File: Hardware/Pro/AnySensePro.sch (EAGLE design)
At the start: 63 parts, among them U1 LP2992IM5-3.3, U2 BLUENRGQTR, U3 SN65HVD232D, U4 STM32F303RET6, U5 BALF-NRG-01D3, U6 M25P16VMN6P, X6 MEM2051-00-195-00-A, X7 TC2030-IDC-NL, Y1 ABM3B, Y2 ABM8, Y3 ABS07

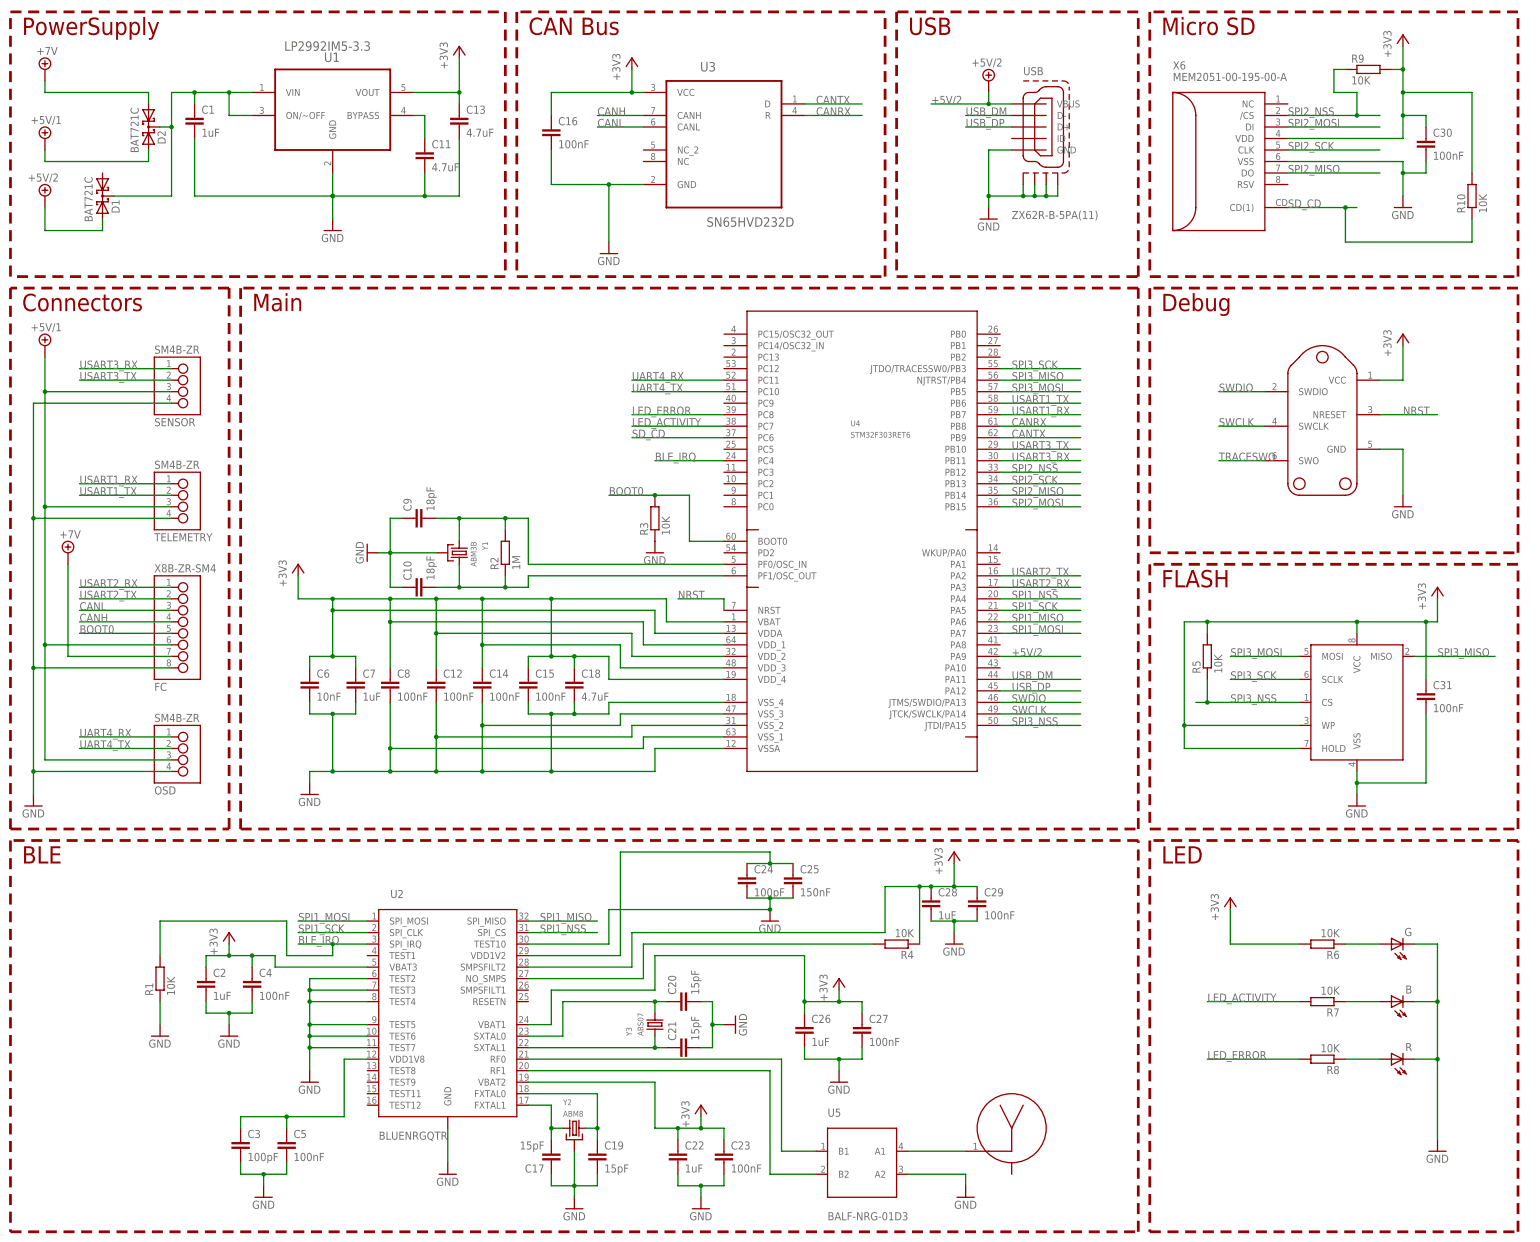
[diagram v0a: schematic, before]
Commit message: Order Codes added
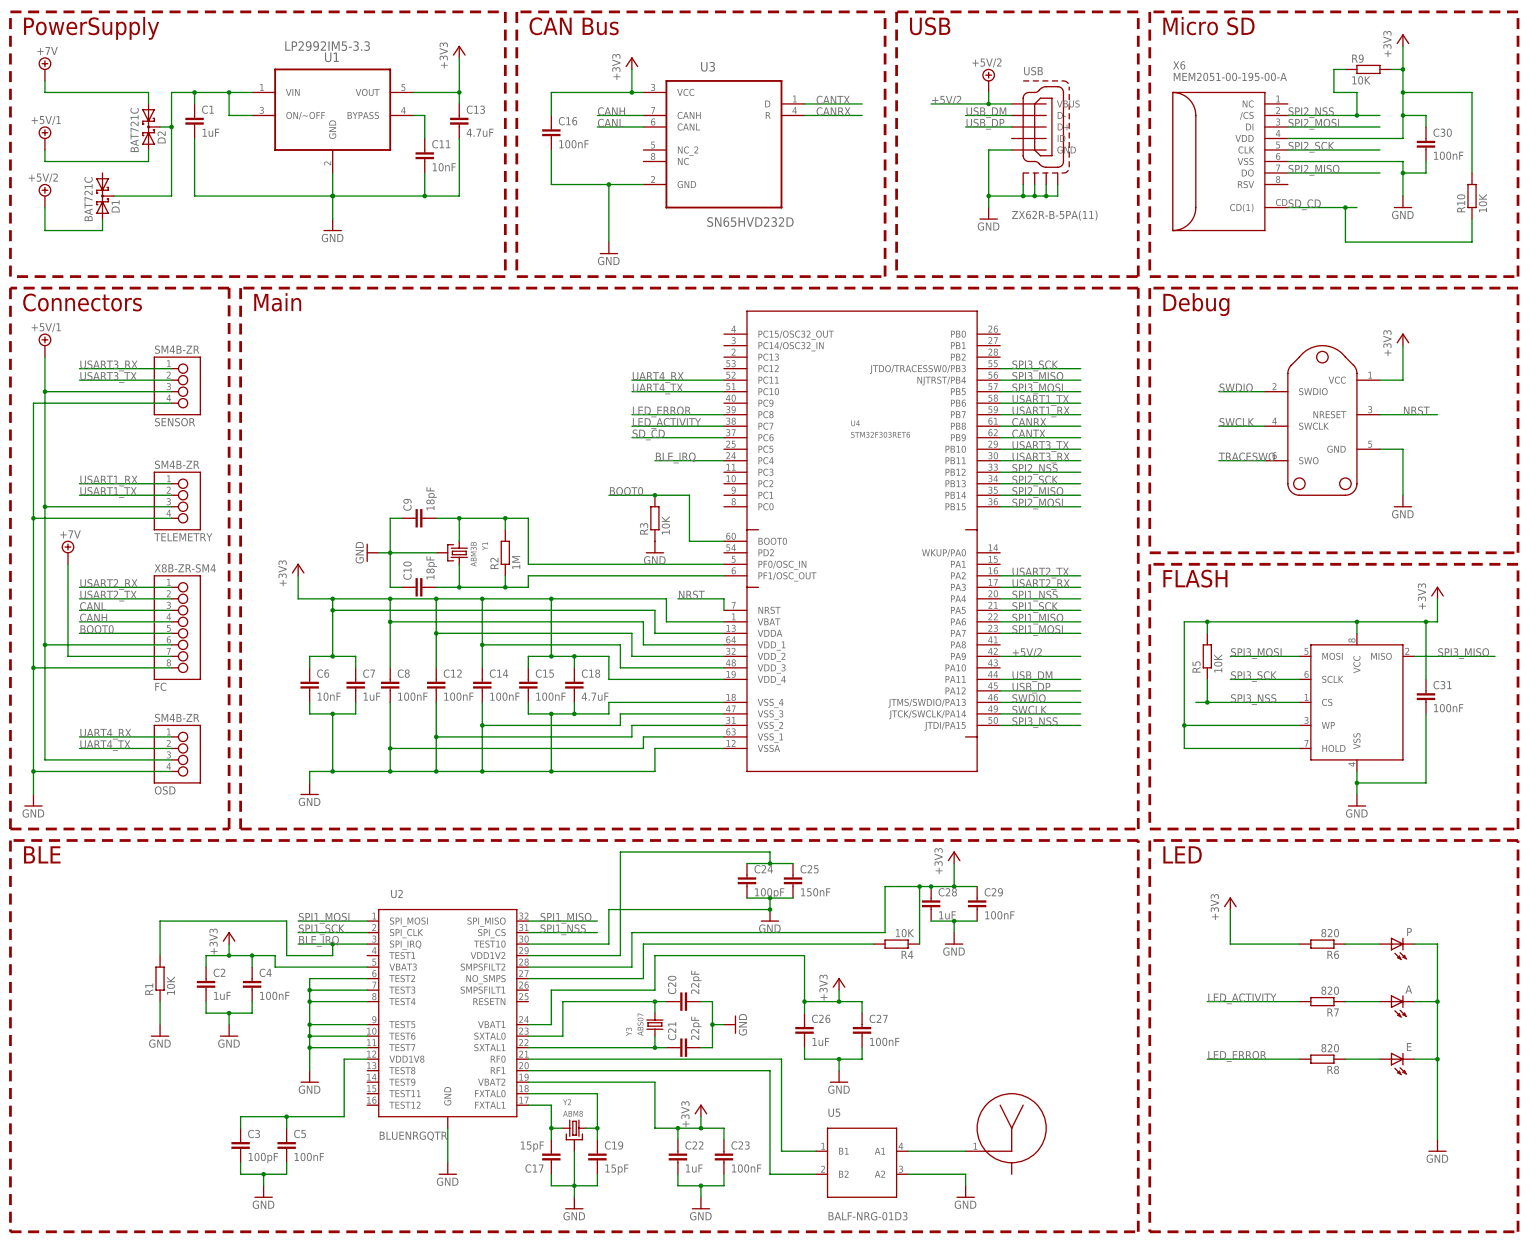
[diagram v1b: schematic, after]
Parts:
- A: OC_FARNELL 2217978 -> 2468793RL
- C1, C2, C22, C26, C28, C7: OC_FARNELL (none) -> 2362093RL
- C10, C9: OC_FARNELL (none) -> 1758947RL
- C11: value 4.7uF -> 10nF; OC_FARNELL (none) -> 1758924RL
- C12, C14, C15, C16, C23, C27, C29, C30, C31, C4, C5: OC_FARNELL (none) -> 1759380RL
- C13, C18: OC_FARNELL (none) -> 2426952RL
- C17, C19: OC_FARNELL (none) -> 1758945RL
- C20, C21: value 15pF -> 22pF; OC_FARNELL (none) -> 1758951RL
- C24, C3: OC_FARNELL (none) -> 2320762RL
- C25: OC_FARNELL (none) -> 2470467RL
- C6: OC_FARNELL (none) -> 1758924RL
- C8: OC_FARNELL test -> 1759380RL
- E: OC_FARNELL 2099224 -> 2468792RL
- P: OC_FARNELL 2099223RL -> 2468791RL
- R1, R10, R3, R4, R5, R9: OC_FARNELL (none) -> 2302739RL
- R2: OC_FARNELL (none) -> 2302957RL
- R6, R7, R8: value 10K -> 820; OC_FARNELL (none) -> 2302628RL
- renumbered B to A, G to P, R to E

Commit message: Hardware redesign
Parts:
- removed A1: 2450AT18A100, johanson-technology:2450AT18A100
- removed C17, C19: 15pF, rcl:C-EUC0402K
- removed C2, C22, C26, C28: 1uF, rcl:C-EUC0402K
- removed C20, C21: 22pF, rcl:C-EUC0402K
- removed C23, C27, C29, C4, C5: 100nF, rcl:C-EUC0402K
- removed C24, C3: 100pF, rcl:C-EUC0402K
- removed C25: 150nF, rcl:C-EUC0402K
- removed U2: BLUENRGQTR, ST-Microelctronics:BLUENRGQTR
- removed U5: BALF-NRG-01D3, ST-Microelctronics:BALF-NRG-01D3
- removed Y2: ABM8, abracon:ABM8-16.000MHZ-10-1-U-T
- removed Y3: ABS07, abracon:ABS.ABS07
- added R11: 22R, rcl:R-EU_R0402
- added R12: 10K, rcl:R-EU_R0402
- added R13: 15K, rcl:R-EU_R0402
- C1: device rcl:C-EUC0402K -> rcl:C-EUC0603K; OC_FARNELL 2362093RL -> 1759409RL
- C13, C18: device rcl:C-EUC0402K -> rcl:C-EUC0603K; OC_FARNELL 2426952RL -> 2320818RL
- C7: OC_FARNELL 2362093RL -> 2320776RL
- R1: value 10K -> 22R
- R4: value 10K -> 1.5K
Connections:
- removed net BLE_IRQ: R1.2, U2.SPI_IRQ, U4.PC4
- removed net N$10: C19.1, U2.FXTAL0, Y2.2
- removed net N$11: C17.2, U2.FXTAL1, Y2.1
- removed net N$12: C3.1, C5.1, U2.VDD1V8
- removed net N$13: C20.1, U2.SXTAL0, Y3.2
- removed net N$14: C21.1, U2.SXTAL1, Y3.1
- removed net N$2: U2.RF0, U5.B1
- removed net N$3: U2.RF1, U5.B2
- removed net N$4: C24.1, C25.1, U2.VDD1V2
- removed net N$5: R4.2, U2.NO_SMPS
- removed net N$9: A1.1, U5.A1
- removed net SPI2_MISO: U4.PB14, X6.DO
- removed net SPI2_MOSI: U4.PB15, X6.DI
- removed net SPI2_NSS: R9.1, U4.PB12, X6./CS
- removed net SPI2_SCK: U4.PB13, X6.CLK
- new net USB_D+: R1.2, R4.1, USBG$1.D+
- new net USB_D-: R11.2, USBG$1.D-
- new net USB_DISCONNECT: R4.2, U4.PA8
- new net USB_SENSE: R12.1, R13.2, U4.PB15
- net +3V3: no longer C2.1, C22.1, C23.1, C26.1, C27.1, C28.1, C29.1, C4.1, R4.1, U2.SMPSFILT2, U2.VBAT1, U2.VBAT2, U2.VBAT3
- net +5V/2: now also R12.2; no longer U4.PA9
- net GND: now also R13.1; no longer C17.1, C19.2, C2.2, C20.2, C21.2, C22.2, C23.2, C24.2, C25.2, C26.2, C27.2, C28.2, C29.2, C3.2, C4.2, C5.2, R1.1, U2.GND, U2.TEST10, U2.TEST2, U2.TEST3, U2.TEST4, U2.TEST5, U2.TEST6, U2.TEST7, U5.A2, Y2.GND
- net LED_ACTIVITY: now also U4.PC3; no longer U4.PC7
- net LED_ERROR: now also U4.PC2; no longer U4.PC8
- net SD_CD: now also U4.PC4; no longer U4.PC6
- net SPI1_MISO: now also X6.DO; no longer U2.SPI_MISO
- net SPI1_MOSI: now also X6.DI; no longer U2.SPI_MOSI
- net SPI1_NSS: now also R9.1, X6./CS; no longer U2.SPI_CS
- net SPI1_SCK: now also X6.CLK; no longer U2.SPI_CLK
- net USART1_RX: now also U4.PA10; no longer U4.PB7
- net USART1_TX: now also U4.PA9; no longer U4.PB6
- net USB_DM: now also R11.1; no longer USBG$1.D-
- net USB_DP: now also R1.1; no longer USBG$1.D+
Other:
- note removed: "BLE"
- moved on the sheet: A, C30, C31, E, P, R1, R10, R4, R5, R6, R7, R8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

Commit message: AnySense Pro V1.1
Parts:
- renumbered TELEMETRY to TELEM
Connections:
- net USB_SENSE: now also U4.PC0; no longer U4.PB15
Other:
- moved on the sheet: R3
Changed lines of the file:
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@@
 <grid distance="0.1" unitdist="inch" unit="inch" style="lines" multiple="1" display="no" altdistance="0.01" altunitdist="inch" altunit="inch"/>
 <layers>
-<layer number="1" name="Top" color="4" fill="1" visible="yes" active="no"/>
-<layer number="16" name="Bottom" color="1" fill="1" visible="yes" active="no"/>
-<layer number="17" name="Pads" color="2" fill="1" visible="yes" active="no"/>
-<layer number="18" name="Vias" color="2" fill="1" visible="yes" active="no"/>
-<layer number="19" name="Unrouted" color="6" fill="1" visible="yes" active="no"/>
-<layer number="20" name="Dimension" color="15" fill="1" visible="yes" active="no"/>
-<layer number="21" name="tPlace" color="7" fill="1" visible="yes" active="no"/>
-<layer number="22" name="bPlace" color="7" fill="1" visible="yes" active="no"/>
-<layer number="23" name="tOrigins" color="15" fill="1" visible="yes" active="no"/>
-<layer number="24" name="bOrigins" color="15" fill="1" visible="yes" active="no"/>
-<layer number="25" name="tNames" color="7" fill="1" visible="yes" active="no"/>
-<layer number="26" name="bNames" color="7" fill="1" visible="yes" active="no"/>
-<layer number="27" name="tValues" color="7" fill="1" visible="yes" active="no"/>
-<layer number="28" name="bValues" color="7" fill="1" visible="yes" active="no"/>
+<layer number="1" name="Top" color="4" fill="1" visible="no" active="no"/>
+<layer number="16" name="Bottom" color="1" fill="1" visible="no" active="no"/>
+<layer number="17" name="Pads" color="2" fill="1" visible="no" active="no"/>
+<layer number="18" name="Vias" color="2" fill="1" visible="no" active="no"/>
+<layer number="19" name="Unrouted" color="6" fill="1" visible="no" active="no"/>
+<layer number="20" name="Dimension" color="15" fill="1" visible="no" active="no"/>
+<layer number="21" name="tPlace" color="7" fill="1" visible="no" active="no"/>
+<layer number="22" name="bPlace" color="7" fill="1" visible="no" active="no"/>
+<layer number="23" name="tOrigins" color="15" fill="1" visible="no" active="no"/>
+<layer number="24" name="bOrigins" color="15" fill="1" visible="no" active="no"/>
+<layer number="25" name="tNames" color="7" fill="1" visible="no" active="no"/>
+<layer number="26" name="bNames" color="7" fill="1" visible="no" active="no"/>
+<layer number="27" name="tValues" color="7" fill="1" visible="no" active="no"/>
+<layer number="28" name="bValues" color="7" fill="1" visible="no" active="no"/>
 <layer number="29" name="tStop" color="7" fill="3" visible="no" active="no"/>
 <layer number="30" name="bStop" color="7" fill="6" visible="no" active="no"/>
@@
 <layer number="35" name="tGlue" color="7" fill="4" visible="no" active="no"/>
 <layer number="36" name="bGlue" color="7" fill="5" visible="no" active="no"/>
-<layer number="37" name="tTest" color="7" fill="1" visible="yes" active="no"/>
-<layer number="38" name="bTest" color="7" fill="1" visible="yes" active="no"/>
+<layer number="37" name="tTest" color="7" fill="1" visible="no" active="no"/>
+<layer number="38" name="bTest" color="7" fill="1" visible="no" active="no"/>
 <layer number="39" name="tKeepout" color="4" fill="11" visible="no" active="no"/>
 <layer number="40" name="bKeepout" color="1" fill="11" visible="no" active="no"/>
@@
 <layer number="44" name="Drills" color="7" fill="1" visible="no" active="no"/>
 <layer number="45" name="Holes" color="7" fill="1" visible="no" active="no"/>
-<layer number="46" name="Milling" color="3" fill="1" visible="yes" active="no"/>
-<layer number="47" name="Measures" color="7" fill="1" visible="yes" active="no"/>
-<layer number="48" name="Document" color="7" fill="1" visible="yes" active="no"/>
-<layer number="49" name="Reference" color="7" fill="1" visible="yes" active="no"/>
-<layer number="50" name="dxf" color="7" fill="1" visible="yes" active="no"/>
-<layer number="51" name="tDocu" color="7" fill="1" visible="yes" active="no"/>
-<layer number="52" name="bDocu" color="7" fill="1" visible="yes" active="no"/>
-<layer number="53" name="tGND_GNDA" color="7" fill="9" visible="yes" active="no"/>
-<layer number="54" name="bGND_GNDA" color="1" fill="9" visible="yes" active="no"/>
-<layer number="56" name="wert" color="7" fill="1" visible="yes" active="no"/>
+<layer number="46" name="Milling" color="3" fill="1" visible="no" active="no"/>
+<layer number="47" name="Measures" color="7" fill="1" visible="no" active="no"/>
+<layer number="48" name="Document" color="7" fill="1" visible="no" active="no"/>
+<layer number="49" name="Reference" color="7" fill="1" visible="no" active="no"/>
+<layer number="50" name="dxf" color="7" fill="1" visible="no" active="no"/>
+<layer number="51" name="tDocu" color="7" fill="1" visible="no" active="no"/>
+<layer number="52" name="bDocu" color="7" fill="1" visible="no" active="no"/>
+<layer number="53" name="tGND_GNDA" color="7" fill="9" visible="no" active="no"/>
+<layer number="54" name="bGND_GNDA" color="1" fill="9" visible="no" active="no"/>
+<layer number="56" name="wert" color="7" fill="1" visible="no" active="no"/>
 <layer number="90" name="Modules" color="5" fill="1" visible="yes" active="yes"/>
 <layer number="91" name="Nets" color="2" fill="1" visible="yes" active="yes"/>
@@
 <parts>
 <part name="X6" library="con-gct" deviceset="MEM2051" device="-00-195-00-A"/>
-<part name="TELEMETRY" library="con-jst" deviceset="?4B-ZR" device="SM"/>
+<part name="TELEM" library="con-jst" deviceset="?4B-ZR" device="SM"/>
 <part name="SENSOR" library="con-jst" deviceset="?4B-ZR" device="SM"/>
 <part name="OSD" library="con-jst" deviceset="?4B-ZR" device="SM"/>
@@
 <instances>
 <instance part="X6" gate="G$1" x="269.24" y="147.32"/>
-<instance part="TELEMETRY" gate="1" x="38.1" y="132.08"/>
+<instance part="TELEM" gate="1" x="38.1" y="132.08"/>
 <instance part="SENSOR" gate="1" x="38.1" y="157.48"/>
 <instance part="OSD" gate="1" x="38.1" y="76.2"/>
@@
 <instance part="FC" gate="G$1" x="38.1" y="106.68"/>
 <instance part="SUPPLY5" gate="G$1" x="12.7" y="121.92"/>
-<instance part="R3" gate="G$1" x="142.24" y="129.54" rot="R90">
-<attribute name="OC_FARNELL" x="142.24" y="129.54" size="1.778" layer="96" rot="R90" display="off"/>
-</instance>
-<instance part="GND12" gate="1" x="142.24" y="121.92"/>
+<instance part="R3" gate="G$1" x="121.92" y="129.54" rot="R90">
+<attribute name="OC_FARNELL" x="121.92" y="129.54" size="1.778" layer="96" rot="R90" display="off"/>
+</instance>
+<instance part="GND12" gate="1" x="121.92" y="121.92"/>
 <instance part="C16" gate="G$1" x="119.38" y="215.9">
 <attribute name="OC_FARNELL" x="119.38" y="215.9" size="1.778" layer="96" display="off"/>
@@
 <segment>
 <pinref part="GND1" gate="1" pin="GND"/>
-<pinref part="TELEMETRY" gate="1" pin="4"/>
+<pinref part="TELEM" gate="1" pin="4"/>
 <wire x1="5.08" y1="68.58" x2="5.08" y2="73.66" width="0.1524" layer="91"/>
 <wire x1="5.08" y1="73.66" x2="5.08" y2="96.52" width="0.1524" layer="91"/>
@@
 <net name="+5V/1" class="0">
 <segment>
-<pinref part="TELEMETRY" gate="1" pin="3"/>
+<pinref part="TELEM" gate="1" pin="3"/>
 <wire x1="35.56" y1="132.08" x2="7.62" y2="132.08" width="0.1524" layer="91"/>
 <wire x1="7.62" y1="132.08" x2="7.62" y2="157.48" width="0.1524" layer="91"/>
@@
 <net name="USART1_RX" class="0">
 <segment>
-<pinref part="TELEMETRY" gate="1" pin="1"/>
+<pinref part="TELEM" gate="1" pin="1"/>
 <wire x1="35.56" y1="137.16" x2="15.24" y2="137.16" width="0.1524" layer="91"/>
 <label x="15.24" y="137.16" size="1.778" layer="95"/>
@@
 <net name="USART1_TX" class="0">
 <segment>
-<pinref part="TELEMETRY" gate="1" pin="2"/>
+<pinref part="TELEM" gate="1" pin="2"/>
 <wire x1="35.56" y1="134.62" x2="15.24" y2="134.62" width="0.1524" layer="91"/>
 <label x="15.24" y="134.62" size="1.778" layer="95"/>
@@
 <segment>
 <pinref part="U4" gate="G$1" pin="BOOT0"/>
-<wire x1="157.48" y1="124.46" x2="149.86" y2="124.46" width="0.1524" layer="91"/>
-<wire x1="149.86" y1="124.46" x2="149.86" y2="134.62" width="0.1524" layer="91"/>
+<wire x1="157.48" y1="124.46" x2="129.54" y2="124.46" width="0.1524" layer="91"/>
+<wire x1="129.54" y1="124.46" x2="129.54" y2="134.62" width="0.1524" layer="91"/>
 <pinref part="R3" gate="G$1" pin="2"/>
-<wire x1="149.86" y1="134.62" x2="142.24" y2="134.62" width="0.1524" layer="91"/>
-<wire x1="142.24" y1="134.62" x2="132.08" y2="134.62" width="0.1524" layer="91"/>
-<junction x="142.24" y="134.62"/>
-<label x="132.08" y="134.62" size="1.778" layer="95"/>
+<wire x1="129.54" y1="134.62" x2="121.92" y2="134.62" width="0.1524" layer="91"/>
+<wire x1="121.92" y1="134.62" x2="111.76" y2="134.62" width="0.1524" layer="91"/>
+<junction x="121.92" y="134.62"/>
+<label x="111.76" y="134.62" size="1.778" layer="95"/>
 </segment>
 <segment>
@@
 </segment>
 <segment>
-<pinref part="U4" gate="G$1" pin="PB15"/>
-<wire x1="218.44" y1="132.08" x2="236.22" y2="132.08" width="0.1524" layer="91"/>
-<label x="220.98" y="132.08" size="1.778" layer="95"/>
-</segment>
-</net>
+<pinref part="U4" gate="G$1" pin="PC0"/>
+<wire x1="157.48" y1="132.08" x2="137.16" y2="132.08" width="0.1524" layer="91"/>
+<label x="137.16" y="132.08" size="1.778" layer="95"/>
+</segment>
+</net>
